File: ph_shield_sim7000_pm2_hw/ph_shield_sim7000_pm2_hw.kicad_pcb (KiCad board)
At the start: 2 copper layers, 70 x 70 mm, 56 parts, among them Q1 C1815, Q2 C1815, Q3 C1815, Q4 C1815, U3 SIM7000E

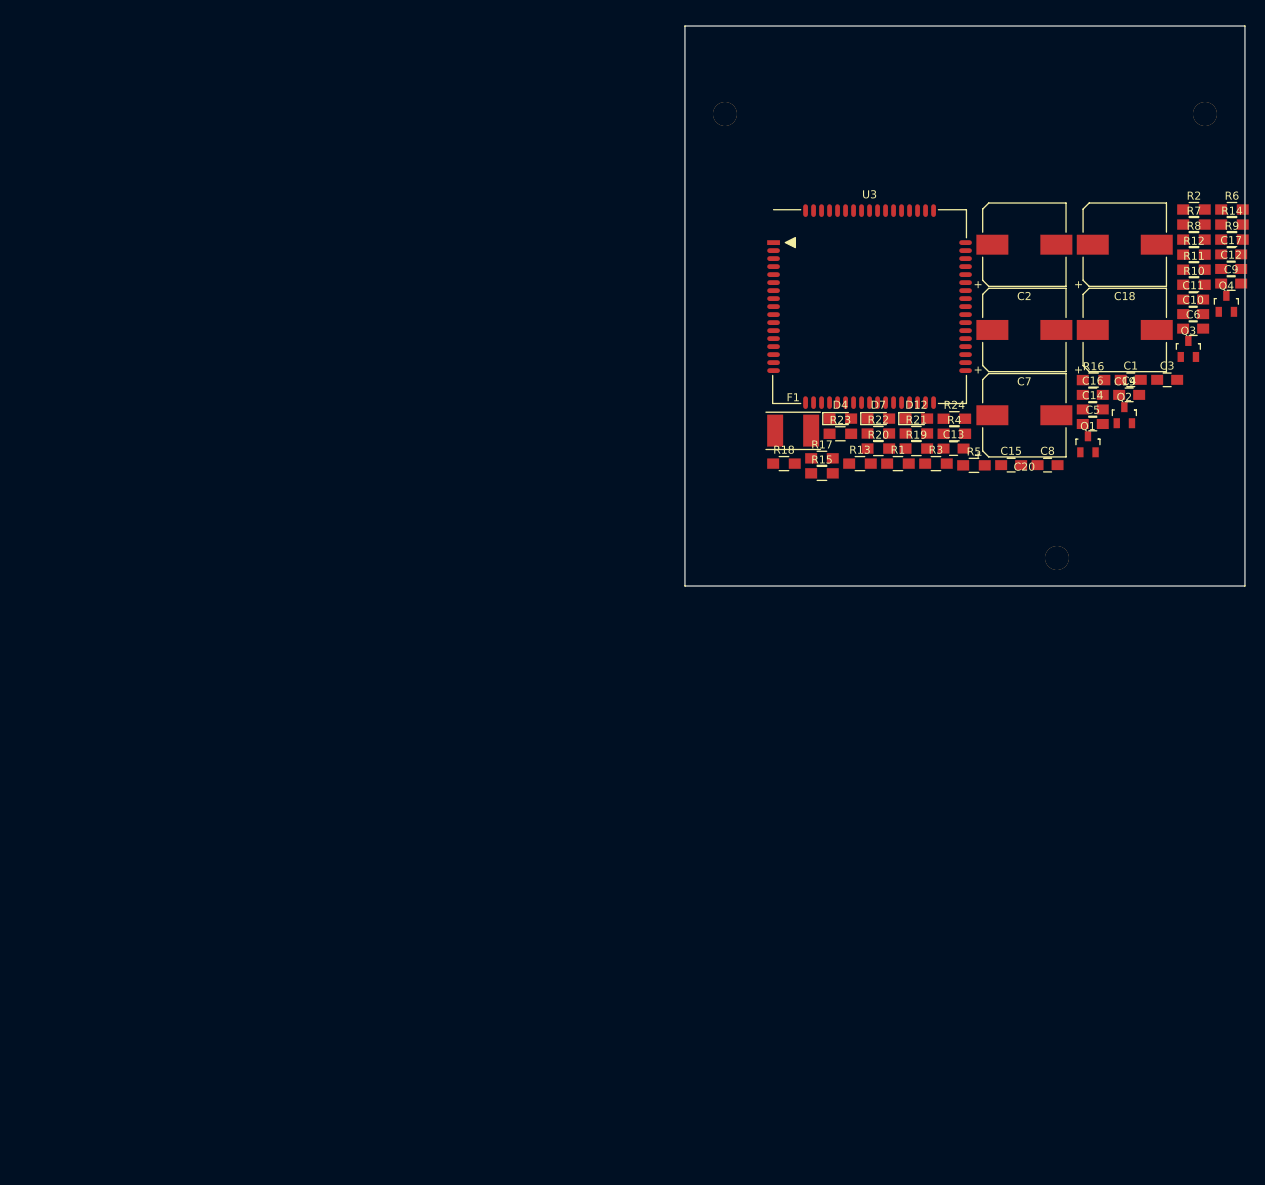
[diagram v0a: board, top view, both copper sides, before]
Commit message: Darwing Layout SIM7000
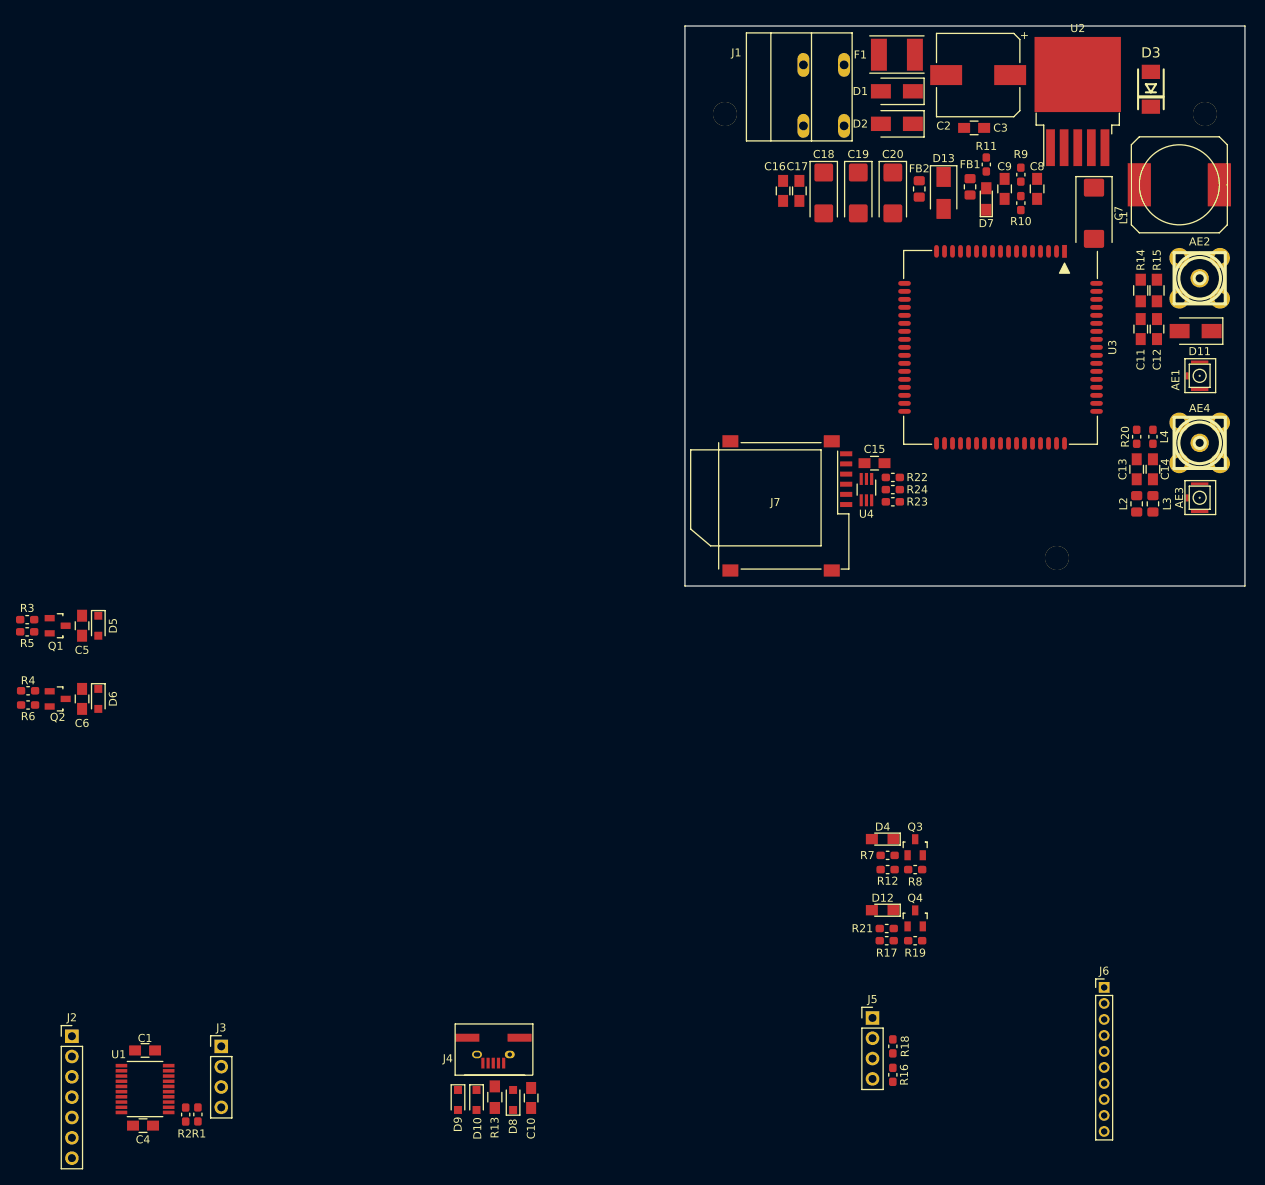
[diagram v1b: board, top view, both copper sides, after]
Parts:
- added AE1: Antenna_Shield, VinhTho_Lib:Anten_GSM_IPEX, F.Cu at (164.3, 93.7)
- added AE2: Antenna_Shield, VinhTho_Lib:Anten_GPS, F.Cu at (164.3, 81.5)
- added AE3: Antenna, VinhTho_Lib:Anten_GSM_IPEX, F.Cu at (164.3, 109.0)
- added AE4: Antenna_Shield, VinhTho_Lib:Anten_GPS, F.Cu at (164.3, 102.1)
- added D1: D_TVS_ALT, VinhTho_Lib:D_SMA_Standard, F.Cu at (126.5, 58.2)
- added D10: ESD, Diode_SMD:D_SOD-323_HandSoldering, F.Cu at (73.9, 184.2)
- added D11: D_TVS_ALT, VinhTho_Lib:D_SMA_Standard, F.Cu at (163.8, 88.1)
- added D13: D_TVS_ALT, VinhTho_Lib:D_SMA_Standard, F.Cu at (132.3, 70.9)
- added D2: D_ALT, VinhTho_Lib:D_SMA_Standard, F.Cu at (126.5, 62.2)
- added D3: MBR360, VinhTho_Lib:DO-214AA, F.Cu at (158.2, 57.9)
- added D5: ESD, Diode_SMD:D_SOD-323_HandSoldering, F.Cu at (26.7, 125.0)
- added D6: ESD, Diode_SMD:D_SOD-323_HandSoldering, F.Cu at (26.7, 134.1)
- added D8: ESD, Diode_SMD:D_SOD-323_HandSoldering, F.Cu at (78.5, 184.2)
- added D9: ESD, Diode_SMD:D_SOD-323_HandSoldering, F.Cu at (71.6, 184.2)
- added FB1: FB101/270R/100Mhz, Resistor_SMD:R_0805_2012Metric_Pad1.15x1.40mm_HandSolder, F.Cu at (135.6, 70.1)
- added FB2: FB101, Resistor_SMD:R_0805_2012Metric_Pad1.15x1.40mm_HandSolder, F.Cu at (129.3, 70.4)
- added J1: Conn_01x02, VinhTho_Lib:TerminalBlock_WAGO-236_2Stift_R5mm_2pol, F.Cu at (114.8, 54.9)
- added J2: Conn_01x07, Connector_PinHeader_2.54mm:PinHeader_1x07_P2.54mm_Vertical, F.Cu at (23.4, 176.3)
- added J3: Conn_01x04, Connector_PinHeader_2.54mm:PinHeader_1x04_P2.54mm_Vertical, F.Cu at (42.0, 177.5)
- added J4: USB_OTG, VinhTho_Lib:USB_Micro-B, F.Cu at (78.1, 178.6)
- added J5: I2C, Connector_PinHeader_2.54mm:PinHeader_1x04_P2.54mm_Vertical, F.Cu at (123.4, 174.0)
- added J6: Conn_01x10, Connector_PinHeader_2.00mm:PinHeader_1x10_P2.00mm_Vertical, F.Cu at (152.4, 170.2)
- added J7: SIM_Card, VinhTho_Lib:socket_sim_6p, F.Cu at (111.8, 109.5)
- added L1: 100uH, VinhTho_Lib:L_, F.Cu at (161.8, 69.8)
- added L2: L, Resistor_SMD:R_0805_2012Metric_Pad1.15x1.40mm_HandSolder, F.Cu at (156.5, 109.7)
- added L3: L, Resistor_SMD:R_0805_2012Metric_Pad1.15x1.40mm_HandSolder, F.Cu at (158.5, 109.7)
- added L4: 47nH, Capacitor_SMD:C_0603_1608Metric_Pad1.05x0.95mm_HandSolder, F.Cu at (158.5, 101.3)
- added U1: TXS0108EPW, Package_SO:TSSOP-20_4.4x6.5mm_P0.65mm, F.Cu at (32.5, 182.9)
- added U2: LM2596S-ADJ, Package_TO_SOT_SMD:TO-263-5_TabPin3, F.Cu at (149.1, 59.4)
- added U4: TVS_Diode_Array_SMF05C, Package_TO_SOT_SMD:SOT-363_SC-70-6_Handsoldering, F.Cu at (122.7, 108.0)
- C14: value 33p -> 33pF
- C18, C19, C20: value 100uF/25V -> 100uF/16V; footprint Capacitors_SMD:CP_Elec_10x10 -> Capacitor_Tantalum_SMD:CP_EIA-6032-28_Kemet-C_Pad2.25x2.35mm_HandSolder
- C7: value 330uF/25V -> 330uF/10V; footprint Capacitors_SMD:CP_Elec_10x10 -> Capacitor_Tantalum_SMD:CP_EIA-7343-30_AVX-N_Pad2.25x2.55mm_HandSolder
- R1, R10, R11, R12, R16, R17, R18, R19, R2, R20, R21, R22, R23, R24, R3, R4, R5, R6, R7, R8, R9: footprint Resistors_SMD:R_0805_HandSoldering -> Resistor_SMD:R_0603_1608Metric_Pad1.05x0.95mm_HandSolder
- R14, R15: value R -> 0R
- moved R2 169.4 mm to (37.6, 186.1), turned to 90 degrees
- moved R6 162.7 mm to (17.9, 134.9), turned to 180 degrees
- moved C4 153.4 mm to (32.3, 187.5), turned to 180 degrees
- moved C1 149.0 mm to (32.5, 178.1), turned to 180 degrees
- moved C6 146.4 mm to (24.6, 134.1), turned to 270 degrees
- moved Q2 138.0 mm to (21.6, 134.1), turned to 270 degrees
- moved Q1 130.8 mm to (21.6, 125.0), turned to 270 degrees
- moved C5 128.8 mm to (24.6, 125.0), turned to 270 degrees
- moved C10 128.3 mm to (80.8, 184.0), turned to 270 degrees
- moved R5 120.2 mm to (17.8, 125.7), turned to 180 degrees
- moved R4 120.2 mm to (17.9, 133.1), turned to 180 degrees
- moved R1 119.5 mm to (39.1, 186.1), turned to 270 degrees
- moved R3 115.3 mm to (17.8, 124.2)
- moved R13 91.4 mm to (76.2, 183.9), turned to 90 degrees
- moved R16 90.4 mm to (126.0, 181.1), turned to 270 degrees
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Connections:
- C1 pad 1: (no net) -> Net-(C1-Pad1)
- C1 pad 2: (no net) -> Net-(C1-Pad2)
- C10 pad 1: (no net) -> Net-(C10-Pad1)
- C14 pad 1: (no net) -> Net-(AE4-Pad1)
- C15 pad 2: (no net) -> Net-(C15-Pad2)
- C16 pad 2: (no net) -> Net-(C16-Pad2)
- C17 pad 2: (no net) -> Net-(C17-Pad2)
- C18 pad 2: (no net) -> Net-(C18-Pad2)
- C19 pad 2: (no net) -> Net-(C19-Pad2)
- C2 pad 2: (no net) -> Net-(C2-Pad2)
- C20 pad 2: (no net) -> Net-(C20-Pad2)
- C3 pad 2: (no net) -> Net-(C3-Pad2)
- C4 pad 1: (no net) -> Net-(C4-Pad1)
- C5 pad 2: (no net) -> Net-(C5-Pad2)
- C6 pad 2: (no net) -> Net-(C6-Pad2)
- C7 pad 2: (no net) -> Net-(C7-Pad2)
- C8 pad 2: (no net) -> Net-(C8-Pad2)
- C9 pad 2: (no net) -> Net-(C9-Pad2)
- D7 pad 1: (no net) -> Net-(D7-Pad1)
- F1 pad 1: (no net) -> Net-(D1-Pad1)
- F1 pad 2: (no net) -> Net-(F1-Pad2)
- Q3 pad 2: (no net) -> Net-(Q3-Pad2)
- Q4 pad 2: (no net) -> Net-(Q4-Pad2)
- R1 pad 1: (no net) -> Net-(R1-Pad1)
- R1 pad 2: (no net) -> Net-(R1-Pad2)
- R10 pad 1: (no net) -> Net-(R10-Pad1)
- R13 pad 2: (no net) -> Net-(J4-Pad1)
- R15 pad 2: (no net) -> Net-(AE2-Pad1)
- R19 pad 2: (no net) -> Net-(R19-Pad2)
- R2 pad 1: (no net) -> Net-(R2-Pad1)
- R2 pad 2: (no net) -> Net-(R2-Pad2)
- R20 pad 2: (no net) -> Net-(L4-Pad1)
- R22 pad 2: (no net) -> Net-(J7-Pad2)
- R23 pad 2: (no net) -> Net-(J7-Pad3)
- R24 pad 2: (no net) -> Net-(J7-Pad7)
- R3 pad 1: (no net) -> /PWR
- R4 pad 2: (no net) -> /RST
- R8 pad 2: (no net) -> Net-(R8-Pad2)
- U3 pad 10: (no net) -> /UART_RX
- U3 pad 11: (no net) -> /PCM_CLK
- U3 pad 12: (no net) -> /PCM_SYNC
- U3 pad 13: (no net) -> /PCM_DIN
- U3 pad 14: (no net) -> /PCM_DOUT
- U3 pad 17: (no net) -> Net-(U3-Pad17)
- U3 pad 18: (no net) -> Net-(U3-Pad18)
- U3 pad 19: (no net) -> Net-(U3-Pad19)
- U3 pad 2: (no net) -> Net-(U3-Pad2)
- U3 pad 20: (no net) -> Net-(U3-Pad20)
- U3 pad 21: (no net) -> Net-(U3-Pad21)
- U3 pad 22: (no net) -> Net-(U3-Pad22)
- U3 pad 23: (no net) -> /LOG_TX
- U3 pad 25: (no net) -> /ADC
- U3 pad 26: (no net) -> Net-(U3-Pad26)
- U3 pad 27: (no net) -> /USB_DP
- U3 pad 28: (no net) -> /USB_DM
- U3 pad 29: (no net) -> Net-(U3-Pad29)
- U3 pad 3: (no net) -> /UART_DTR
- U3 pad 34: (no net) -> /SIM_DET
- U3 pad 35: (no net) -> Net-(U3-Pad35)
- U3 pad 36: (no net) -> Net-(U3-Pad36)
- U3 pad 39: (no net) -> Net-(U3-Pad39)
- U3 pad 4: (no net) -> /UART_RI
- U3 pad 40: (no net) -> Net-(U3-Pad40)
- U3 pad 41: (no net) -> Net-(U3-Pad41)
- U3 pad 42: (no net) -> Net-(U3-Pad42)
- U3 pad 43: (no net) -> Net-(U3-Pad43)
- U3 pad 44: (no net) -> Net-(U3-Pad44)
- U3 pad 47: (no net) -> Net-(U3-Pad47)
- U3 pad 48: (no net) -> /GPIO4
- U3 pad 49: (no net) -> /UART3_RX
- U3 pad 5: (no net) -> /UART_DCD
- U3 pad 50: (no net) -> /UART3_TX
- U3 pad 51: (no net) -> Net-(U3-Pad51)
- U3 pad 54: (no net) -> Net-(U3-Pad54)
- U3 pad 6: (no net) -> /BOOT_CFG
- U3 pad 67: (no net) -> /GPIO2
- U3 pad 68: (no net) -> /GPIO3
- U3 pad 7: (no net) -> /UART_CTS
- U3 pad 8: (no net) -> /UART_RTS
- U3 pad 9: (no net) -> /UART_TX

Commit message: Design Schematic SIM7000E
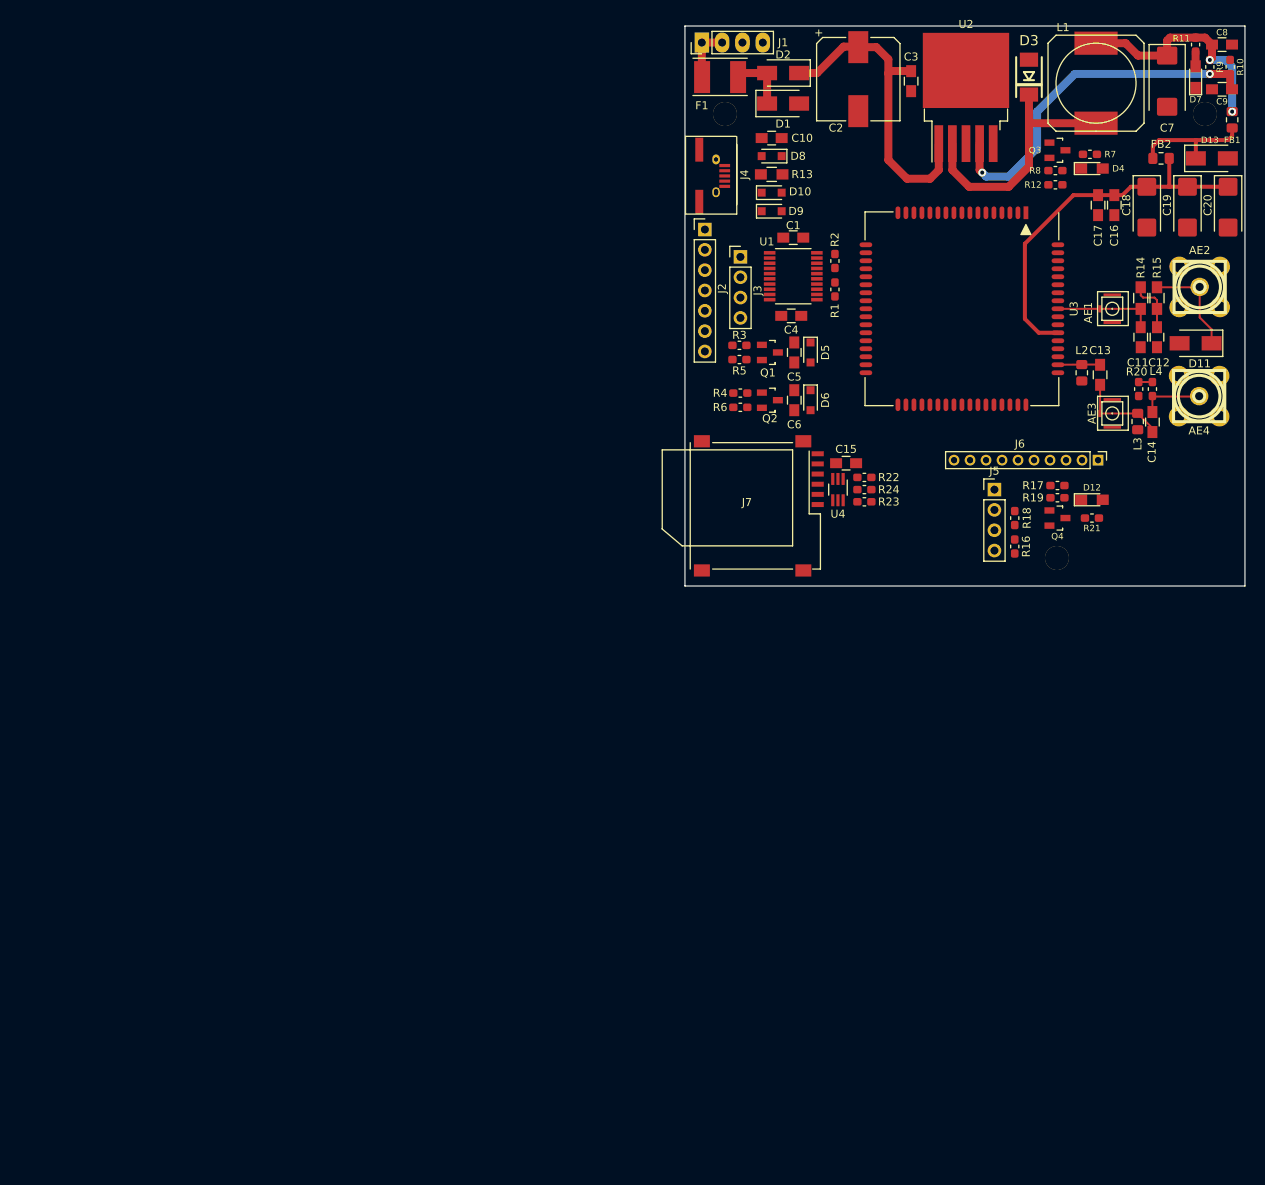
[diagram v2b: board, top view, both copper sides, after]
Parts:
- J1: value Conn_01x02 -> Conn_01x04; footprint VinhTho_Lib:TerminalBlock_WAGO-236_2Stift_R5mm_2pol -> VinhTho_Lib:Header-4pin-2.54
- moved R2 134.1 mm to (118.7, 79.4), turned to 270 degrees
- moved R1 130.3 mm to (118.7, 82.9)
- moved C1 130.0 mm to (113.5, 76.5)
- moved U1 130.0 mm to (113.5, 81.3)
- moved C4 129.7 mm to (113.3, 86.2)
- moved J2 128.2 mm to (102.5, 75.4)
- moved C10 123.7 mm to (110.8, 64.0), turned to 0 degrees
- moved D8 122.3 mm to (110.8, 66.3), turned to 180 degrees
- moved R13 120.4 mm to (110.8, 68.5), turned to 180 degrees
- moved D10 119.3 mm to (110.8, 70.8), turned to 0 degrees
- moved J3 118.1 mm to (106.9, 78.9)
- moved D9 117.8 mm to (110.8, 73.2), turned to 0 degrees
- moved J4 114.8 mm to (103.9, 66.7), turned to 270 degrees
- moved C6 96.5 mm to (113.7, 96.8)
- moved D6 96.5 mm to (115.7, 96.8)
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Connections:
- AE1 pad 2: Net-(AE1-Pad2) -> GND
- AE2 pad 2: Net-(AE2-Pad2) -> GND
- AE4 pad 2: Net-(AE4-Pad2) -> GND
- C1 pad 1: Net-(C1-Pad1) -> +3V3
- C1 pad 2: Net-(C1-Pad2) -> GND
- C10 pad 1: Net-(C10-Pad1) -> GND
- C11 pad 2: Net-(C11-Pad2) -> GND
- C12 pad 2: Net-(C11-Pad2) -> GND
- C15 pad 2: Net-(C15-Pad2) -> GND
- C16 pad 2: Net-(C16-Pad2) -> GND
- C17 pad 2: Net-(C17-Pad2) -> GND
- C18 pad 2: Net-(C18-Pad2) -> GND
- C19 pad 2: Net-(C19-Pad2) -> GND
- C2 pad 2: Net-(C2-Pad2) -> GND
- C20 pad 2: Net-(C20-Pad2) -> GND
- C3 pad 2: Net-(C3-Pad2) -> GND
- C4 pad 1: Net-(C4-Pad1) -> GND
- C6 pad 2: Net-(C6-Pad2) -> GND
- C7 pad 2: Net-(C7-Pad2) -> GND
- C8 pad 2: Net-(C8-Pad2) -> GND
- C9 pad 2: Net-(C9-Pad2) -> GND
- D1 pad 2: Net-(D1-Pad2) -> GND
- D10 pad 2: Net-(D10-Pad2) -> GND
- D11 pad 2: Net-(D11-Pad2) -> GND
- D13 pad 2: Net-(D13-Pad2) -> GND
- D3 pad 2: Net-(D3-Pad2) -> GND
- D6 pad 2: Net-(D6-Pad2) -> GND
- D7 pad 1: Net-(D7-Pad1) -> GND
- D8 pad 2: Net-(D8-Pad2) -> GND
- D9 pad 2: Net-(D9-Pad2) -> GND
- J1 pad 2: Net-(J1-Pad2) -> Net-(F1-Pad2)
- J2 pad 1: Net-(J2-Pad1) -> +3V3
- J2 pad 2: Net-(J2-Pad2) -> GND
- J4 pad 5: Net-(J4-Pad5) -> GND
- J4 pad 6: Net-(J4-Pad5) -> GND
- J5 pad 2: Net-(J5-Pad2) -> GND
- J6 pad 10: Net-(J6-Pad10) -> GND
- J7 pad 5: Net-(J7-Pad5) -> GND
- L2 pad 2: Net-(L2-Pad2) -> GND
- L3 pad 2: Net-(L3-Pad2) -> GND
- Q2 pad 2: Net-(Q2-Pad2) -> GND
- Q3 pad 2: Net-(Q3-Pad2) -> GND
- Q4 pad 2: Net-(Q4-Pad2) -> GND
- R1 pad 2: Net-(R1-Pad2) -> GND
- R10 pad 1: Net-(R10-Pad1) -> GND
- R19 pad 2: Net-(R19-Pad2) -> GND
- R2 pad 1: Net-(R2-Pad1) -> GND
- R6 pad 1: Net-(Q2-Pad2) -> GND
- R8 pad 2: Net-(R8-Pad2) -> GND
- U1 pad 11: Net-(U1-Pad11) -> GND
- U1 pad 19: Net-(C1-Pad1) -> +3V3
- U2 pad 3: Net-(U2-Pad3) -> GND
- U2 pad 5: Net-(U2-Pad5) -> GND
- U3 pad 17: Net-(U3-Pad17) -> GND
- U3 pad 39: Net-(U3-Pad39) -> GND
- U3 pad 45: Net-(U3-Pad45) -> GND
- U3 pad 46: Net-(U3-Pad45) -> GND
- U3 pad 54: Net-(U3-Pad54) -> GND
- U3 pad 58: Net-(U3-Pad58) -> GND
- U3 pad 59: Net-(U3-Pad58) -> GND
- U3 pad 61: Net-(U3-Pad61) -> GND
- U3 pad 62: Net-(U3-Pad61) -> GND
- U3 pad 63: Net-(U3-Pad61) -> GND
- U3 pad 64: Net-(U3-Pad61) -> GND
- U3 pad 65: Net-(U3-Pad61) -> GND
- U4 pad 2: Net-(U4-Pad2) -> GND
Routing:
- net /VBAT: track 0.00 -> 46.1 mm
- net Net-(C9-Pad1): track 0.00 -> 45.0 mm, vias 0 -> 2
- net Net-(C2-Pad1): track 0.00 -> 39.8 mm
- net Net-(D3-Pad1): track 0.00 -> 32.3 mm
- net Net-(C7-Pad1): track 0.00 -> 28.3 mm, vias 0 -> 2
- net VDD: track 0.00 -> 15.3 mm
- net Net-(AE2-Pad1): track 0.00 -> 13.0 mm
- net Net-(AE1-Pad1): track 0.00 -> 12.6 mm
- net Net-(AE3-Pad1): track 0.00 -> 11.5 mm
- net Net-(AE4-Pad1): track 0.00 -> 7.80 mm
- net Net-(D1-Pad1): track 0.00 -> 7.64 mm
- net Net-(F1-Pad2): track 0.00 -> 6.87 mm
- net Net-(C12-Pad1): track 0.00 -> 6.67 mm
- net Net-(C13-Pad2): track 0.00 -> 5.32 mm
- net Net-(D7-Pad2): track 0.00 -> 1.84 mm
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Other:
- net class 0.5 added: clearance 0.2, trace_width 0.25, via_dia 1, via_drill 0.5

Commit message: SIM7000E
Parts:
- moved R24 3.10 mm to (124.2, 110.5)
- moved R23 1.93 mm to (124.2, 108.7)
- moved R22 1.85 mm to (124.2, 106.9)
- moved C15 1.78 mm to (121.9, 104.8)
- moved U4 1.14 mm to (120.1, 108.5)
- moved R1 0.51 mm to (119.3, 82.9), turned to 90 degrees
- moved R2 0.51 mm to (119.3, 79.4)
- turned R5 to 0 degrees
- turned R6 to 0 degrees
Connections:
- Q1 pad 2: Net-(Q1-Pad2) -> GND
- R5 pad 1: Net-(Q1-Pad2) -> GND
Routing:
- net /SIM_DATA: track 0.00 -> 24.4 mm
- net /SIM_VDD: track 0.00 -> 23.6 mm
- net /SIM_CLK: track 0.00 -> 19.8 mm
- net Net-(J7-Pad3): track 0.00 -> 17.9 mm, vias 0 -> 2
- net /SIM_RST: track 0.00 -> 15.9 mm
- net Net-(R12-Pad2): track 0.00 -> 12.6 mm
- net Net-(R2-Pad2): track 0.00 -> 12.3 mm, vias 0 -> 2
- net Net-(J7-Pad7): track 0.00 -> 11.6 mm
- net /VDD_EXT: track 0.00 -> 11.1 mm
- net Net-(J7-Pad2): track 0.00 -> 9.66 mm
- net Net-(Q3-Pad1): track 0.00 -> 8.33 mm
- net /RST: track 0.00 -> 8.17 mm
- net VDD: track 15.3 -> 22.1 mm
- net Net-(C5-Pad1): track 0.00 -> 5.18 mm
- net Net-(C6-Pad1): track 0.00 -> 5.13 mm
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
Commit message: SIM7000E layouting
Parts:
- turned R21 to 180 degrees
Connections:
- J7 pad 0: (no net) -> GND
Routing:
- net /VDD_EXT: track 11.1 -> 64.1 mm, vias 0 -> 1
- net VDD: track 22.1 -> 69.3 mm, vias 0 -> 3
- net /UART_RI: track 0.00 -> 45.0 mm, vias 0 -> 2
- net Net-(R17-Pad1): track 0.00 -> 39.3 mm, vias 0 -> 2
- net /UART_DCD: track 0.00 -> 35.9 mm, vias 0 -> 2
- net /ADC: track 0.00 -> 35.2 mm, vias 0 -> 2
- net /UART_DTR: track 0.00 -> 35.0 mm, vias 0 -> 2
- net /BOOT_CFG: track 0.00 -> 33.9 mm, vias 0 -> 1
- net /LOG_TX: track 0.00 -> 33.5 mm, vias 0 -> 1
- net /UART_TX: track 0.00 -> 33.4 mm, vias 0 -> 2
- net /GPIO3: track 0.00 -> 30.9 mm, vias 0 -> 1
- net /GPIO2: track 0.00 -> 30.9 mm, vias 0 -> 1
- net /UART_CTS: track 0.00 -> 30.6 mm, vias 0 -> 2
- net /UART_RX: track 0.00 -> 30.3 mm, vias 0 -> 2
- net /UART_RTS: track 0.00 -> 28.9 mm, vias 0 -> 2
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- added copper zone on B.Cu, net GND
- added copper zone on F.Cu, net GND
